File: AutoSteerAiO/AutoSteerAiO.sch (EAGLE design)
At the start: 86 parts, among them J4 CONNECTOR 1x5 PINS, K4 CB1A-P-12V, T1 BC547, U1 VX7805-1000

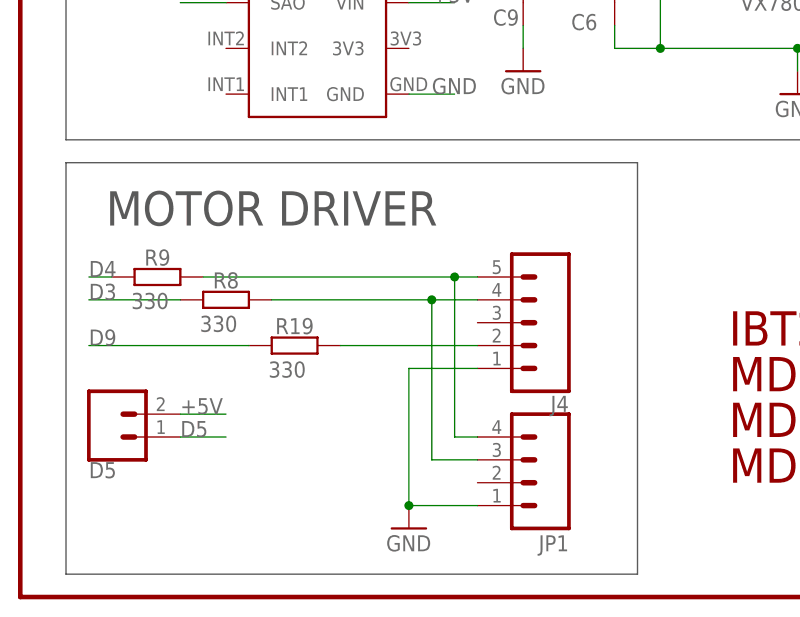
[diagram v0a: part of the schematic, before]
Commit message: Add files via upload
One connector for all motor drivers
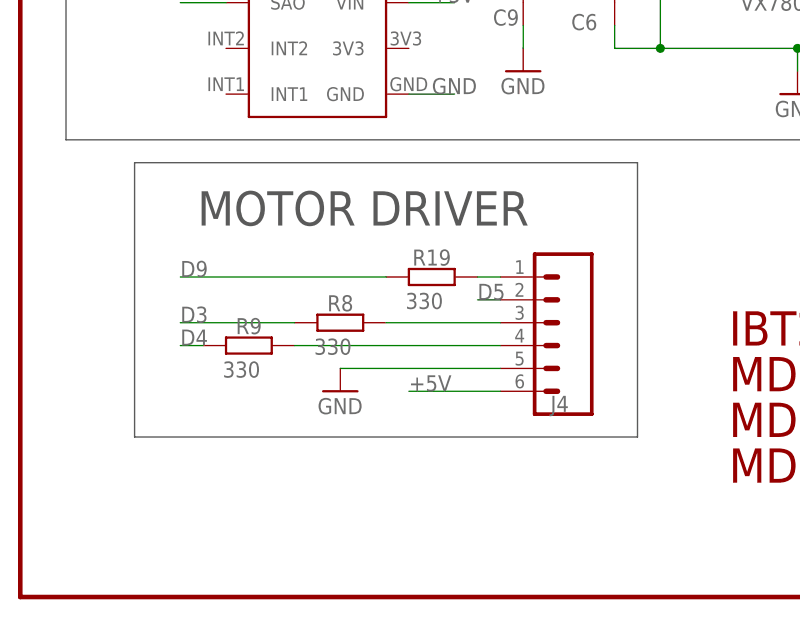
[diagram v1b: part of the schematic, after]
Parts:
- removed D5: CONNECTOR 1x1 PIN, SparkFun-Connectors:CONN_02
- removed JP1: CONNECTOR 1x4 PINS, Header and Connector:2600-04_(NORMAL)
- J4: device Header and Connector:2600-05_(NORMAL) -> SparkFun-Connectors:CONN_06SILK_FEMALE_PTH
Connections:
- net +5V: now also J4.6; no longer D5.2
- net D5: now also J4.2; no longer D5.1
- net GND: now also J4.5; no longer J4.1, JP1.1
- net N$19: now also J4.4; no longer J4.5, JP1.4
- net N$20: now also J4.3; no longer J4.4, JP1.3
- net N$22: now also J4.1; no longer J4.2
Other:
- moved on the sheet: R19, R8, R9

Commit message: Add files via upload
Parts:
- removed 15V1, 15V2, GND, GND30: WIREPAD4,16O1,6, wirepad:WIREPAD4,16O1,6
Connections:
- net +15V: no longer 15V1.P, 15V2.P
- net GND: no longer GND.P, GND30.P
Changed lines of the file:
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@@
 <attribute name="OC_NEWARK" value="unknown"/>
 </part>
-<part name="15V1" library="wirepad" library_urn="urn:adsk.eagle:library:412" deviceset="WIREPAD" device="4,16O1,6" package3d_urn="urn:adsk.eagle:package:30843/1">
-<attribute name="MF" value=""/>
-<attribute name="MPN" value=""/>
-<attribute name="OC_NEWARK" value="unknown"/>
-</part>
-<part name="15V2" library="wirepad" library_urn="urn:adsk.eagle:library:412" deviceset="WIREPAD" device="4,16O1,6" package3d_urn="urn:adsk.eagle:package:30843/1">
-<attribute name="MF" value=""/>
-<attribute name="MPN" value=""/>
-<attribute name="OC_NEWARK" value="unknown"/>
-</part>
-<part name="GND" library="wirepad" library_urn="urn:adsk.eagle:library:412" deviceset="WIREPAD" device="4,16O1,6" package3d_urn="urn:adsk.eagle:package:30843/1">
-<attribute name="MF" value=""/>
-<attribute name="MPN" value=""/>
-<attribute name="OC_NEWARK" value="unknown"/>
-</part>
-<part name="GND30" library="wirepad" library_urn="urn:adsk.eagle:library:412" deviceset="WIREPAD" device="4,16O1,6" package3d_urn="urn:adsk.eagle:package:30843/1">
-<attribute name="MF" value=""/>
-<attribute name="MPN" value=""/>
-<attribute name="OC_NEWARK" value="unknown"/>
-</part>
-<part name="GND22" library="supply1" library_urn="urn:adsk.eagle:library:371" deviceset="GND" device=""/>
 <part name="J4" library="SparkFun-Connectors" library_urn="urn:adsk.eagle:library:513" deviceset="CONN_06" device="SILK_FEMALE_PTH" package3d_urn="urn:adsk.eagle:package:38009/1" value="CONNECTOR 1x5 PINS">
 <attribute name="MF" value=""/>
@@
 <attribute name="MPN" x="10.16" y="241.3" size="1.778" layer="96" display="off"/>
 </instance>
-<instance part="15V1" gate="G$1" x="53.34" y="275.59" smashed="yes" rot="R270">
-<attribute name="NAME" x="55.1942" y="276.733" size="1.778" layer="95" rot="R270"/>
-<attribute name="OC_NEWARK" x="53.34" y="275.59" size="1.778" layer="96" display="off"/>
-<attribute name="MF" x="53.34" y="275.59" size="1.778" layer="96" display="off"/>
-<attribute name="MPN" x="53.34" y="275.59" size="1.778" layer="96" display="off"/>
-</instance>
-<instance part="15V2" gate="G$1" x="58.42" y="275.59" smashed="yes" rot="R270">
-<attribute name="NAME" x="60.2742" y="276.733" size="1.778" layer="95" rot="R270"/>
-<attribute name="OC_NEWARK" x="58.42" y="275.59" size="1.778" layer="96" display="off"/>
-<attribute name="MF" x="58.42" y="275.59" size="1.778" layer="96" display="off"/>
-<attribute name="MPN" x="58.42" y="275.59" size="1.778" layer="96" display="off"/>
-</instance>
-<instance part="GND" gate="G$1" x="66.04" y="275.59" smashed="yes" rot="R270">
-<attribute name="NAME" x="67.8942" y="276.733" size="1.778" layer="95" rot="R270"/>
-<attribute name="OC_NEWARK" x="66.04" y="275.59" size="1.778" layer="96" display="off"/>
-<attribute name="MF" x="66.04" y="275.59" size="1.778" layer="96" display="off"/>
-<attribute name="MPN" x="66.04" y="275.59" size="1.778" layer="96" display="off"/>
-</instance>
-<instance part="GND30" gate="G$1" x="71.12" y="275.59" smashed="yes" rot="R270">
-<attribute name="NAME" x="72.9742" y="276.733" size="1.778" layer="95" rot="R270"/>
-<attribute name="OC_NEWARK" x="71.12" y="275.59" size="1.778" layer="96" display="off"/>
-<attribute name="MF" x="71.12" y="275.59" size="1.778" layer="96" display="off"/>
-<attribute name="MPN" x="71.12" y="275.59" size="1.778" layer="96" display="off"/>
-</instance>
-<instance part="GND22" gate="1" x="71.12" y="254" smashed="yes">
-<attribute name="VALUE" x="68.58" y="251.46" size="1.778" layer="96"/>
-</instance>
 <instance part="J4" gate="G$1" x="58.42" y="93.98" smashed="yes" rot="R180">
 <attribute name="NAME" x="60.96" y="85.852" size="1.778" layer="95" font="vector" rot="R180"/>
@@
 <pinref part="C4" gate="G$1" pin="-"/>
 <pinref part="GND21" gate="1" pin="GND"/>
-</segment>
-<segment>
-<pinref part="GND22" gate="1" pin="GND"/>
-<wire x1="66.04" y1="269.24" x2="71.12" y2="269.24" width="0.1524" layer="91"/>
-<pinref part="GND30" gate="G$1" pin="P"/>
-<wire x1="71.12" y1="273.05" x2="71.12" y2="269.24" width="0.1524" layer="91"/>
-<junction x="71.12" y="269.24"/>
-<pinref part="GND" gate="G$1" pin="P"/>
-<wire x1="66.04" y1="273.05" x2="66.04" y2="269.24" width="0.1524" layer="91"/>
-<wire x1="71.12" y1="269.24" x2="71.12" y2="256.54" width="0.1524" layer="91"/>
 </segment>
 <segment>
@@
 <pinref part="P+1" gate="1" pin="+15V"/>
 <pinref part="C4" gate="G$1" pin="+"/>
-<junction x="48.26" y="269.24"/>
-<wire x1="48.26" y1="269.24" x2="48.26" y2="271.78" width="0.1524" layer="91"/>
-<pinref part="15V1" gate="G$1" pin="P"/>
-<wire x1="53.34" y1="273.05" x2="53.34" y2="269.24" width="0.1524" layer="91"/>
-<pinref part="15V2" gate="G$1" pin="P"/>
-<wire x1="53.34" y1="269.24" x2="58.42" y2="269.24" width="0.1524" layer="91"/>
-<wire x1="58.42" y1="269.24" x2="58.42" y2="273.05" width="0.1524" layer="91"/>
-<wire x1="53.34" y1="269.24" x2="48.26" y2="269.24" width="0.1524" layer="91"/>
-<junction x="53.34" y="269.24"/>
-<junction x="48.26" y="269.24"/>
 <pinref part="D2" gate="1" pin="A"/>
 <pinref part="K4" gate="2" pin="P"/>
@@
 <wire x1="43.18" y1="269.24" x2="43.18" y2="266.7" width="0.1524" layer="91"/>
 <wire x1="43.18" y1="266.7" x2="43.18" y2="243.84" width="0.1524" layer="91"/>
-<wire x1="48.26" y1="269.24" x2="48.26" y2="266.7" width="0.1524" layer="91"/>
+<wire x1="48.26" y1="271.78" x2="48.26" y2="266.7" width="0.1524" layer="91"/>
 <wire x1="43.18" y1="266.7" x2="48.26" y2="266.7" width="0.1524" layer="91"/>
 <junction x="43.18" y="266.7"/>

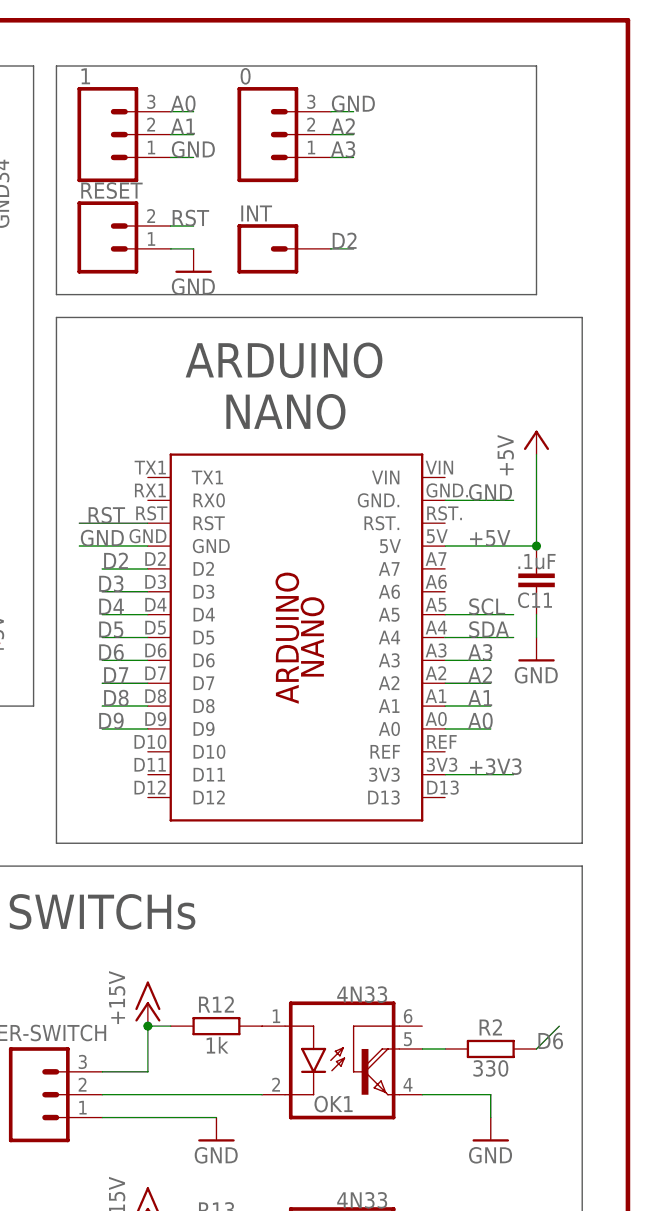
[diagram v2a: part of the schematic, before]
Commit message: Add files via upload
Added connector for SWEncoder
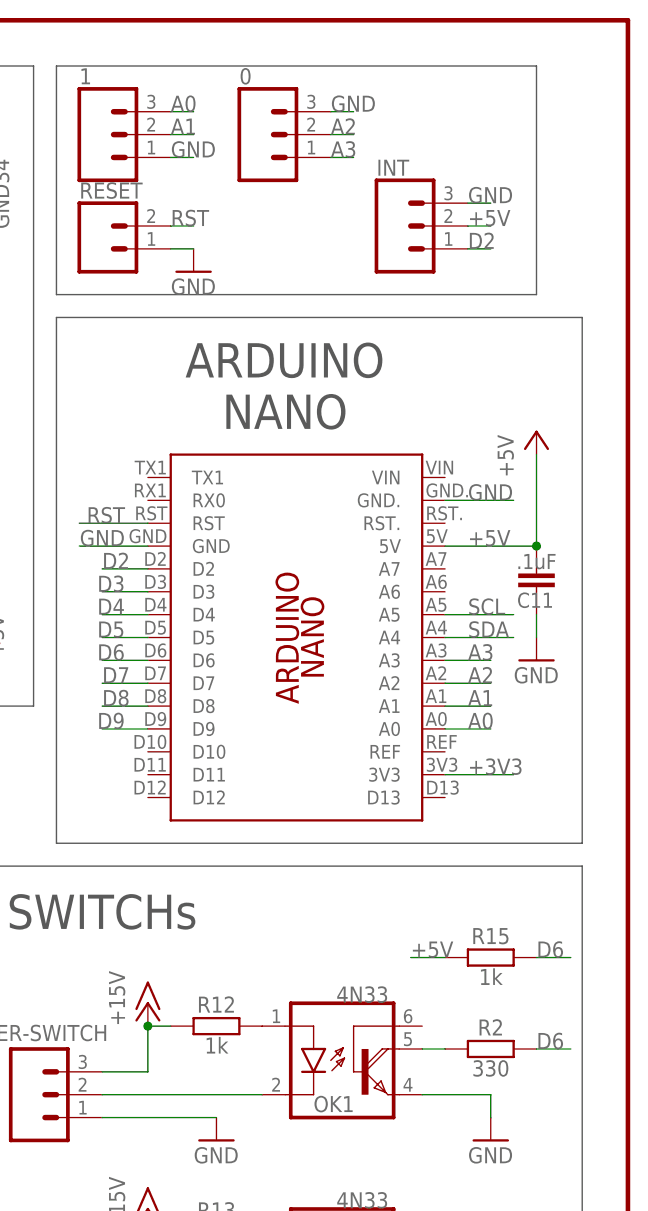
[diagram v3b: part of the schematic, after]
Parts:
- added R15: 1k, resistor:R-EU_0207/7
- INT: value CONNECTOR 1x1 PIN -> (none); device SparkFun-Connectors:CONN_01 -> SparkFun-Connectors:CONN_03; OC_NEWARK unknown -> (none)
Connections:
- net +5V: now also INT.2, R15.1
- net D6: now also R15.2
- net GND: now also INT.3
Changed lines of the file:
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@@
 <?xml version="1.0" encoding="utf-8"?>
 <!DOCTYPE eagle SYSTEM "eagle.dtd">
-<eagle version="9.3.2">
+<eagle version="9.4.0">
 <drawing>
 <settings>
@@
 </part>
 <part name="GND13" library="supply1" library_urn="urn:adsk.eagle:library:371" deviceset="GND" device=""/>
-<part name="INT" library="SparkFun-Connectors" library_urn="urn:adsk.eagle:library:513" deviceset="CONN_01" device="" package3d_urn="urn:adsk.eagle:package:38028/1" value="CONNECTOR 1x1 PIN">
-<attribute name="MF" value=""/>
-<attribute name="MPN" value=""/>
-<attribute name="OC_NEWARK" value="unknown"/>
-</part>
 <part name="U$4" library="#Motor Drivers" deviceset="IBT2" device="">
 <attribute name="MF" value=""/>
@@
 <attribute name="OC_NEWARK" value="unknown"/>
 </part>
+<part name="R15" library="resistor" library_urn="urn:adsk.eagle:library:348" deviceset="R-EU_" device="0207/7" package3d_urn="urn:adsk.eagle:package:23493/2" value="1k">
+<attribute name="MF" value=""/>
+<attribute name="MPN" value=""/>
+<attribute name="OC_NEWARK" value="unknown"/>
+</part>
+<part name="INT" library="SparkFun-Connectors" library_urn="urn:adsk.eagle:library:513" deviceset="CONN_03" device="" package3d_urn="urn:adsk.eagle:package:38063/1"/>
 </parts>
 <sheets>
@@
 <attribute name="VALUE" x="68.58" y="218.44" size="1.778" layer="96"/>
 </instance>
-<instance part="INT" gate="G$1" x="170.18" y="264.16" smashed="yes">
-<attribute name="NAME" x="167.64" y="267.208" size="1.778" layer="95" font="vector"/>
-<attribute name="OC_NEWARK" x="170.18" y="264.16" size="1.778" layer="96" rot="R90" display="off"/>
-<attribute name="MF" x="170.18" y="264.16" size="1.778" layer="96" rot="R90" display="off"/>
-<attribute name="MPN" x="170.18" y="264.16" size="1.778" layer="96" rot="R90" display="off"/>
-</instance>
 <instance part="U$4" gate="G$1" x="78.74" y="91.44" smashed="yes">
 <attribute name="OC_NEWARK" x="78.74" y="91.44" size="1.778" layer="96" display="off"/>
@@
 <attribute name="MF" x="20.32" y="250.19" size="1.778" layer="96" rot="R180" display="off"/>
 <attribute name="MPN" x="20.32" y="250.19" size="1.778" layer="96" rot="R180" display="off"/>
+</instance>
+<instance part="R15" gate="G$1" x="195.58" y="185.42" smashed="yes">
+<attribute name="NAME" x="195.58" y="186.9186" size="1.778" layer="95" rot="R180" align="top-center"/>
+<attribute name="VALUE" x="195.58" y="184.15" size="1.778" layer="95" rot="R180" align="bottom-center"/>
+<attribute name="OC_NEWARK" x="195.58" y="185.42" size="1.778" layer="96" display="off"/>
+<attribute name="MF" x="195.58" y="185.42" size="1.778" layer="96" display="off"/>
+<attribute name="MPN" x="195.58" y="185.42" size="1.778" layer="96" display="off"/>
+</instance>
+<instance part="INT" gate="J$1" x="185.42" y="266.7" smashed="yes">
+<attribute name="VALUE" x="182.88" y="259.334" size="1.778" layer="96" font="vector"/>
+<attribute name="NAME" x="182.88" y="272.288" size="1.778" layer="95" font="vector"/>
 </instance>
 </instances>
@@
 <wire x1="53.34" y1="86.36" x2="43.18" y2="86.36" width="0.1524" layer="91"/>
 <label x="43.18" y="86.36" size="1.778" layer="95"/>
+</segment>
+<segment>
+<pinref part="R15" gate="G$1" pin="1"/>
+<wire x1="190.5" y1="185.42" x2="186.69" y2="185.42" width="0.1524" layer="91"/>
+<label x="186.69" y="185.42" size="1.778" layer="95" rot="R180" align="top-right"/>
+</segment>
+<segment>
+<pinref part="INT" gate="J$1" pin="2"/>
+<wire x1="193.04" y1="266.7" x2="195.58" y2="266.7" width="0.1524" layer="91"/>
+<label x="193.04" y="266.7" size="1.778" layer="95"/>
 </segment>
 </net>
@@
 <wire x1="33.02" y1="220.98" x2="33.02" y2="222.25" width="0.1524" layer="91"/>
 </segment>
+<segment>
+<pinref part="INT" gate="J$1" pin="3"/>
+<wire x1="193.04" y1="269.24" x2="195.58" y2="269.24" width="0.1524" layer="91"/>
+<label x="193.04" y="269.24" size="1.778" layer="95"/>
+</segment>
 </net>
 <net name="D5" class="0">
@@
 <segment>
 <pinref part="R2" gate="G$1" pin="2"/>
-<wire x1="200.66" y1="175.26" x2="203.2" y2="177.8" width="0.1524" layer="91"/>
+<wire x1="200.66" y1="175.26" x2="204.47" y2="175.26" width="0.1524" layer="91"/>
 <label x="200.66" y="175.26" size="1.778" layer="95"/>
+</segment>
+<segment>
+<pinref part="R15" gate="G$1" pin="2"/>
+<wire x1="204.47" y1="185.42" x2="200.66" y2="185.42" width="0.1524" layer="91"/>
+<label x="200.66" y="185.42" size="1.778" layer="95" rot="R180" align="top-right"/>
 </segment>
 </net>
@@
 <net name="D2" class="0">
 <segment>
-<pinref part="INT" gate="G$1" pin="1"/>
-<wire x1="177.8" y1="264.16" x2="180.34" y2="264.16" width="0.1524" layer="91"/>
-<label x="177.8" y="264.16" size="1.778" layer="95" rot="R180" align="top-right"/>
-</segment>
-<segment>
 <pinref part="PCB1" gate="G$1" pin="D2"/>
 <wire x1="157.48" y1="228.6" x2="152.4" y2="228.6" width="0.1524" layer="91"/>
 <label x="152.4" y="228.6" size="1.778" layer="95"/>
 </segment>
-</net>
+<segment>
+<pinref part="INT" gate="J$1" pin="1"/>
+<wire x1="193.04" y1="264.16" x2="195.58" y2="264.16" width="0.1524" layer="91"/>
+<label x="193.04" y="264.16" size="1.778" layer="95"/>
+</segment>
+</net>
